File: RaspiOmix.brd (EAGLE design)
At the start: 85 x 56 mm, 49 parts, among them IC1 MCP3424-E/SL, IC2 DS1307

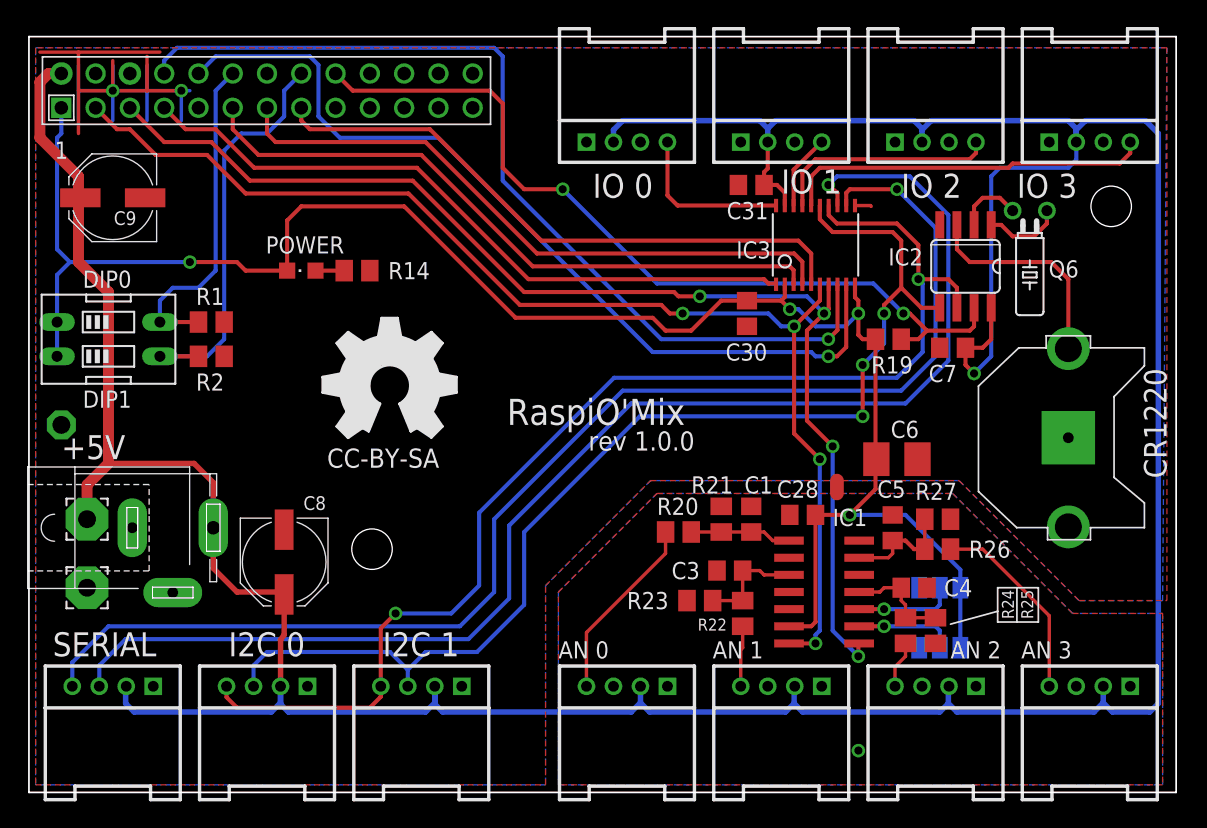
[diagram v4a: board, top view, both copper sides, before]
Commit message: Version 1.0.1
Hole size modification
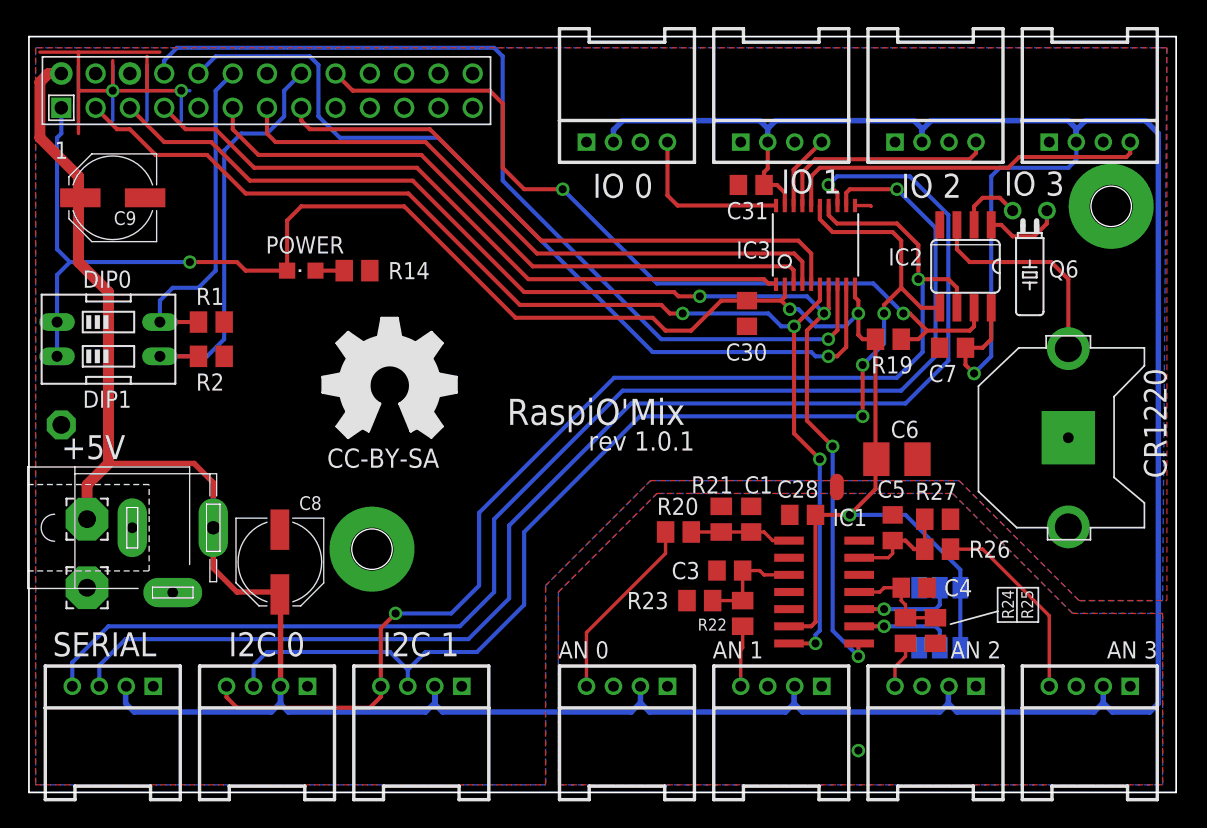
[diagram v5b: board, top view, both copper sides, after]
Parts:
- moved C8 0.32 mm to (18.7, 17.1)
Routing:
- net +5V: track 282.9 -> 283.5 mm
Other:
- board text added: "rev 1.0.1"
- board text removed: "rev 1.0.0"
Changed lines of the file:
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@@
 <setting verticaltext="up"/>
 </settings>
-<grid distance="12.5" unitdist="mil" unit="mil" style="dots" multiple="1" display="yes" altdistance="0.025" altunitdist="inch" altunit="inch"/>
+<grid distance="25" unitdist="mil" unit="mil" style="dots" multiple="1" display="yes" altdistance="0.025" altunitdist="inch" altunit="inch"/>
 <layers>
 <layer number="1" name="Top" color="4" fill="1" visible="yes" active="yes"/>
@@
 <board>
 <plain>
-<circle x="25.55875" y="18.0975" radius="2.129853125" width="1.016" layer="17"/>
-<circle x="80.3275" y="43.4975" radius="2.06984375" width="1.016" layer="17"/>
 <text x="2.54" y="24.765" size="1.778" layer="25">+5V</text>
 <text x="26.3525" y="10.16" size="1.778" layer="25">I2C 1</text>
@@
 <text x="55.88" y="44.45" size="1.778" layer="25">IO 1</text>
 <text x="64.77" y="44.1325" size="1.778" layer="25">IO 2</text>
-<text x="73.3425" y="44.1325" size="1.778" layer="25">IO 3</text>
+<text x="72.39" y="44.29125" size="1.778" layer="25">IO 3</text>
 <text x="39.37" y="10.00125" size="1.27" layer="25">AN 0</text>
 <text x="50.8" y="10.00125" size="1.27" layer="25">AN 1</text>
 <text x="68.42125" y="10.00125" size="1.27" layer="25">AN 2</text>
-<text x="73.66" y="10.00125" size="1.27" layer="25">AN 3</text>
+<text x="80.01" y="10.00125" size="1.27" layer="25">AN 3</text>
 <wire x1="73.3425" y1="12.7" x2="74.93" y2="12.7" width="0.127" layer="25"/>
 <wire x1="74.93" y1="12.7" x2="74.93" y2="15.24" width="0.127" layer="25"/>
@@
 <text x="4.1275" y="37.465" size="1.27" layer="25">DIP0</text>
 <text x="4.1275" y="28.575" size="1.27" layer="25">DIP1</text>
-<text x="41.5925" y="25.4" size="1.4224" layer="25">rev 1.0.0</text>
+<text x="41.5925" y="25.4" size="1.4224" layer="25">rev 1.0.1</text>
 <text x="35.56" y="27.305" size="1.9304" layer="25">RaspiO'Mix</text>
 <text x="22.225" y="24.13" size="1.4224" layer="25">CC-BY-SA </text>
@@
 <attribute name="VALUE" x="69.85" y="35.56" size="1.27" layer="27" rot="R180"/>
 </element>
-<element name="C8" library="rcl" package="PANASONIC_D" value="220uf" x="19.05" y="17.145" smashed="yes" rot="R270">
-<attribute name="NAME" x="20.475" y="21.0025" size="1.016" layer="25"/>
-<attribute name="VALUE" x="17.075" y="18.895" size="1.016" layer="27" rot="R270"/>
+<element name="C8" library="rcl" package="PANASONIC_D" value="220uf" x="18.7325" y="17.145" smashed="yes" rot="R270">
+<attribute name="NAME" x="20.1575" y="21.0025" size="1.016" layer="25"/>
+<attribute name="VALUE" x="16.7575" y="18.895" size="1.016" layer="27" rot="R270"/>
 </element>
 <element name="C9" library="rcl" package="PANASONIC_D" value="220uf" x="6.35" y="44.1325" rot="R180"/>
@@
 <wire x1="7.3025" y1="8.255" x2="7.3025" y2="6.6675" width="0.4064" layer="16"/>
 <wire x1="7.3025" y1="6.6675" x2="7.9375" y2="6.0325" width="0.4064" layer="16"/>
-<wire x1="18.78" y1="7.9375" x2="18.78" y2="11.3825" width="0.4064" layer="1"/>
-<wire x1="18.78" y1="11.3825" x2="19.05" y2="11.7475" width="0.4064" layer="1"/>
 <wire x1="13.795" y1="19.685" x2="13.795" y2="16.685" width="0.4064" layer="1"/>
 <wire x1="13.795" y1="16.685" x2="15.5575" y2="14.9225" width="0.4064" layer="1"/>
@@
 <contactref element="C9" pad="+"/>
 <contactref element="C8" pad="+"/>
-<wire x1="19.05" y1="14.745" x2="19.05" y2="11.7475" width="0.4064" layer="1"/>
 <wire x1="3.81" y1="44.2725" x2="3.95" y2="44.1325" width="0.6096" layer="1"/>
 <wire x1="3.81" y1="43.9925" x2="3.95" y2="44.1325" width="0.6096" layer="1"/>
@@
 <wire x1="12.3825" y1="24.4475" x2="13.795" y2="23.035" width="0.4064" layer="1"/>
 <wire x1="13.795" y1="19.685" x2="13.795" y2="23.035" width="0.4064" layer="1"/>
+<wire x1="18.7325" y1="14.745" x2="18.78" y2="14.745" width="0.4064" layer="1"/>
+<wire x1="18.78" y1="14.745" x2="18.78" y2="7.9375" width="0.4064" layer="1"/>
+<wire x1="18.7325" y1="14.745" x2="18.3575" y2="14.745" width="0.4064" layer="1"/>
+<wire x1="18.3575" y1="14.745" x2="18.3575" y2="14.9225" width="0.4064" layer="1"/>
 <wire x1="3.81" y1="45.72" x2="3.81" y2="44.2725" width="0" layer="19" extent="1-1"/>
-<wire x1="19.05" y1="14.745" x2="18.3575" y2="14.9225" width="0" layer="19" extent="1-1"/>
 </signal>
 <signal name="SDA">
@@
 <contactref element="CON_IO_3" pad="4"/>
 <wire x1="81.74" y1="48.26" x2="81.74" y2="47.45" width="0.3048" layer="1"/>
-<wire x1="81.74" y1="47.45" x2="80.9625" y2="46.6725" width="0.3048" layer="1"/>
-<wire x1="80.9625" y1="46.6725" x2="73.025" y2="46.6725" width="0.3048" layer="1"/>
-<wire x1="73.025" y1="46.6725" x2="72.7075" y2="46.355" width="0.3048" layer="1"/>
+<wire x1="81.74" y1="47.45" x2="81.43875" y2="47.14875" width="0.3048" layer="1"/>
+<wire x1="81.43875" y1="47.14875" x2="73.50125" y2="47.14875" width="0.3048" layer="1"/>
+<wire x1="73.50125" y1="47.14875" x2="72.7075" y2="46.355" width="0.3048" layer="1"/>
 <wire x1="72.7075" y1="46.355" x2="58.7375" y2="46.355" width="0.3048" layer="1"/>
 <wire x1="58.7375" y1="46.355" x2="58.1025" y2="45.72" width="0.3048" layer="1"/>
@@
 <via x="63.5" y="13.6525" extent="1-16" drill="0.6" diameter="1.016"/>
 </signal>
+<signal name="N$9">
+<via x="25.55875" y="18.0975" extent="1-16" drill="3.2" diameter="6.3"/>
+</signal>
+<signal name="N$10">
+<via x="80.3275" y="43.4975" extent="1-16" drill="3.2" diameter="6.3"/>
+</signal>
 </signals>

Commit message: PCB
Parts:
- R14: value 1k -> 470
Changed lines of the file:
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@@
 <setting verticaltext="up"/>
 </settings>
-<grid distance="25" unitdist="mil" unit="mil" style="dots" multiple="1" display="yes" altdistance="0.025" altunitdist="inch" altunit="inch"/>
+<grid distance="12.5" unitdist="mil" unit="mil" style="dots" multiple="1" display="yes" altdistance="0.025" altunitdist="inch" altunit="inch"/>
 <layers>
 <layer number="1" name="Top" color="4" fill="1" visible="yes" active="yes"/>
@@
 <text x="68.42125" y="10.00125" size="1.27" layer="25">AN 2</text>
 <text x="80.01" y="10.00125" size="1.27" layer="25">AN 3</text>
-<wire x1="73.3425" y1="12.7" x2="74.93" y2="12.7" width="0.127" layer="25"/>
-<wire x1="74.93" y1="12.7" x2="74.93" y2="15.24" width="0.127" layer="25"/>
-<wire x1="74.93" y1="15.24" x2="73.3425" y2="15.24" width="0.127" layer="25"/>
-<wire x1="73.3425" y1="15.24" x2="71.91375" y2="15.24" width="0.127" layer="25"/>
-<wire x1="71.91375" y1="15.24" x2="71.91375" y2="13.49375" width="0.127" layer="25"/>
-<wire x1="71.91375" y1="13.49375" x2="71.91375" y2="12.7" width="0.127" layer="25"/>
-<wire x1="71.91375" y1="12.7" x2="73.3425" y2="12.7" width="0.127" layer="25"/>
-<wire x1="73.3425" y1="12.7" x2="73.3425" y2="15.24" width="0.127" layer="25"/>
+<wire x1="73.3425" y1="12.3825" x2="74.93" y2="12.3825" width="0.127" layer="25"/>
+<wire x1="74.93" y1="12.3825" x2="74.93" y2="15.5575" width="0.127" layer="25"/>
+<wire x1="74.93" y1="15.5575" x2="73.3425" y2="15.5575" width="0.127" layer="25"/>
+<wire x1="73.3425" y1="15.5575" x2="71.91375" y2="15.5575" width="0.127" layer="25"/>
+<wire x1="71.91375" y1="15.5575" x2="71.91375" y2="13.49375" width="0.127" layer="25"/>
+<wire x1="71.91375" y1="13.49375" x2="71.91375" y2="12.3825" width="0.127" layer="25"/>
+<wire x1="71.91375" y1="12.3825" x2="73.3425" y2="12.3825" width="0.127" layer="25"/>
+<wire x1="73.3425" y1="12.3825" x2="73.3425" y2="15.5575" width="0.127" layer="25"/>
 <wire x1="68.42125" y1="12.54125" x2="71.91375" y2="13.49375" width="0.127" layer="25"/>
 <text x="4.1275" y="37.465" size="1.27" layer="25">DIP0</text>
@@
 <attribute name="VALUE" x="21.59" y="41.275" size="1.27" layer="27" rot="R180"/>
 </element>
-<element name="R14" library="rcl" package="M0805" value="1k" x="24.4475" y="38.735" smashed="yes" rot="R180">
+<element name="R14" library="rcl" package="M0805" value="470" x="24.4475" y="38.735" smashed="yes" rot="R180">
 <attribute name="NAME" x="29.845" y="39.37" size="1.27" layer="25" rot="R180"/>
 <attribute name="VALUE" x="25.7175" y="41.275" size="1.27" layer="27" rot="R180"/>
@@
 <wire x1="78.4225" y1="49.8475" x2="82.8675" y2="49.8475" width="0.4064" layer="16"/>
 <wire x1="82.8675" y1="49.8475" x2="83.82" y2="48.895" width="0.4064" layer="16"/>
-<wire x1="83.82" y1="48.895" x2="83.82" y2="6.6675" width="0.4064" layer="16"/>
+<wire x1="83.82" y1="48.895" x2="83.82" y2="46.6725" width="0.4064" layer="16"/>
+<wire x1="83.82" y1="46.6725" x2="84.1375" y2="46.355" width="0.4064" layer="16"/>
+<wire x1="84.1375" y1="46.355" x2="84.1375" y2="40.64" width="0.4064" layer="16"/>
+<wire x1="84.1375" y1="40.64" x2="83.82" y2="40.3225" width="0.4064" layer="16"/>
+<wire x1="83.82" y1="40.3225" x2="83.82" y2="6.6675" width="0.4064" layer="16"/>
 <wire x1="83.82" y1="6.6675" x2="83.185" y2="6.0325" width="0.4064" layer="16"/>
 <wire x1="83.185" y1="6.0325" x2="80.4225" y2="6.0325" width="0.4064" layer="16"/>
